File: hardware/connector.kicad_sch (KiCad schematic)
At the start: 2 parts

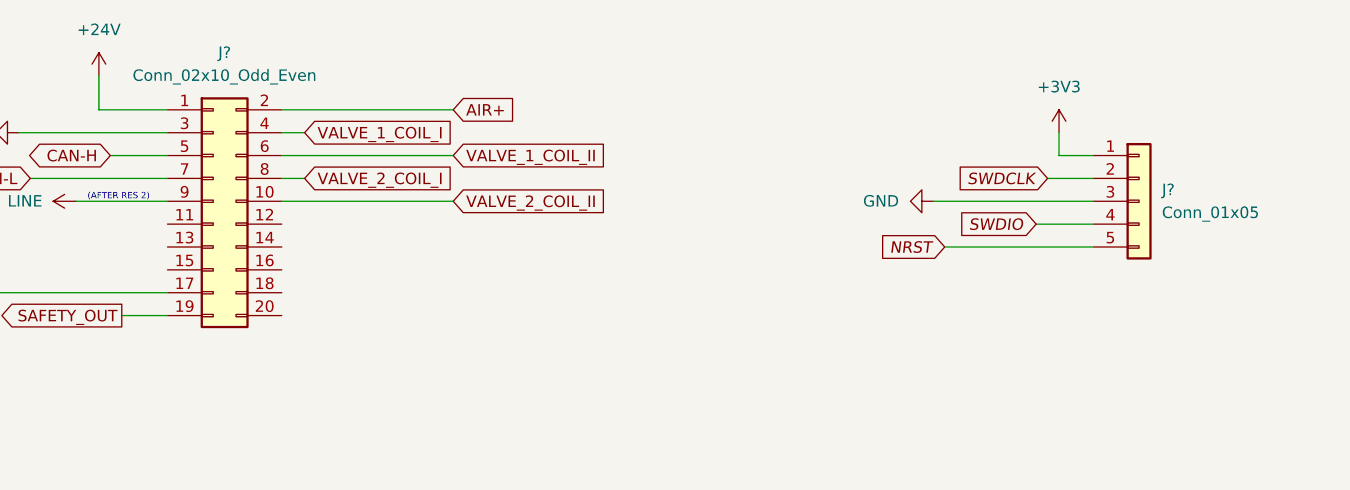
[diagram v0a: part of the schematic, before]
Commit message: Schematic ready for second review
Cleaned up, numerated, added footprints, JW notes considered
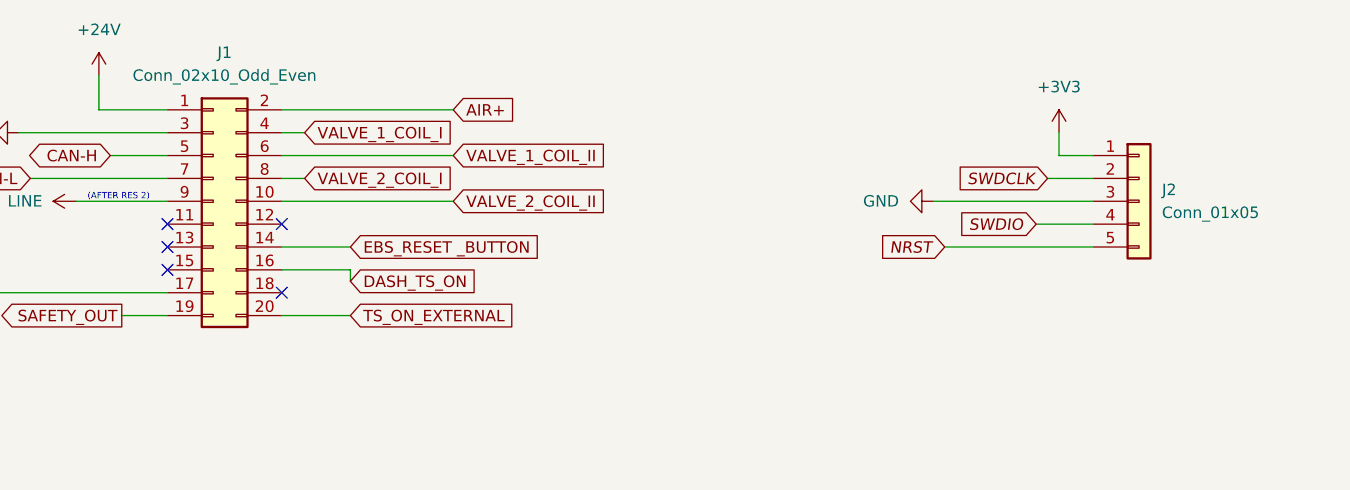
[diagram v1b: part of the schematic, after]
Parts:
- gave numbers to parts that had none: 2
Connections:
- net EBS_RESET _BUTTON: now reaches J1.14 (Pin_14)
- net DASH_TS_ON: now reaches J1.16 (Pin_16)
- net TS_ON_EXTERNAL: now reaches J1.20 (Pin_20)
- no-connect marks 0 -> 5
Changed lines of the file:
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@@
     (company "PUT Motorsport")
   )
+  (no_connect (at 128.27 92.71))
+  (no_connect (at 128.27 85.09))
+  (no_connect (at 115.57 85.09))
+  (no_connect (at 115.57 87.63))
+  (no_connect (at 115.57 90.17))
   (wire (pts (xy 128.27 77.47) (xy 147.32 77.47))
     (stroke (width 0) (type default) (color 0 0 0 0))
@@
     (stroke (width 0) (type default) (color 0 0 0 0))
   )
+  (wire (pts (xy 128.27 95.25) (xy 135.89 95.25))
+    (stroke (width 0) (type default) (color 0 0 0 0))
+  )
   (wire (pts (xy 99.06 74.93) (xy 115.57 74.93))
     (stroke (width 0) (type default) (color 0 0 0 0))
   )
+  (wire (pts (xy 128.27 90.17) (xy 135.89 90.17))
+    (stroke (width 0) (type default) (color 0 0 0 0))
+  )
   (wire (pts (xy 218.44 77.47) (xy 214.63 77.47))
     (stroke (width 0) (type default) (color 0 0 0 0))
@@
   )
   (wire (pts (xy 212.09 85.09) (xy 218.44 85.09))
+    (stroke (width 0) (type default) (color 0 0 0 0))
+  )
+  (wire (pts (xy 128.27 87.63) (xy 135.89 87.63))
+    (stroke (width 0) (type default) (color 0 0 0 0))
+  )
+  (wire (pts (xy 135.89 90.17) (xy 135.89 91.44))
     (stroke (width 0) (type default) (color 0 0 0 0))
   )
@@
     )
   )
+  (global_label "DASH_TS_ON" (shape input) (at 135.89 91.44 0) (fields_autoplaced)
+    (effects (font (size 1.27 1.27)) (justify left))
+    (property "Intersheet References" "${INTERSHEET_REFS}" (id 0) (at 149.975 91.5194 0)
+      (effects (font (size 1.27 1.27)) (justify left) hide)
+    )
+  )
   (global_label "VALVE_1_COIL_I" (shape input) (at 130.81 74.93 0) (fields_autoplaced)
     (effects (font (size 1.27 1.27)) (justify left))
@@
     )
   )
+  (global_label "TS_ON_EXTERNAL" (shape input) (at 135.89 95.25 0) (fields_autoplaced)
+    (effects (font (size 1.27 1.27)) (justify left))
+    (property "Intersheet References" "${INTERSHEET_REFS}" (id 0) (at 154.2688 95.3294 0)
+      (effects (font (size 1.27 1.27)) (justify left) hide)
+    )
+  )
+  (global_label "EBS_RESET _BUTTON" (shape input) (at 135.89 87.63 0) (fields_autoplaced)
+    (effects (font (size 1.27 1.27)) (justify left))
+    (property "Intersheet References" "${INTERSHEET_REFS}" (id 0) (at 157.7764 87.7094 0)
+      (effects (font (size 1.27 1.27)) (justify left) hide)
+    )
+  )
   (global_label "SAFETY_OUT" (shape output) (at 110.49 95.25 180) (fields_autoplaced)
     (effects (font (size 1.27 1.27)) (justify right))
@@
   (symbol (lib_id "power:+3V3") (at 214.63 74.93 0) (unit 1)
     (in_bom yes) (on_board yes) (fields_autoplaced)
-    (property "Reference" "#PWR?" (id 0) (at 214.63 78.74 0)
+    (property "Reference" "#PWR049" (id 0) (at 214.63 78.74 0)
       (effects (font (size 1.27 1.27)) hide)
     )
@@
   (symbol (lib_id "power:+24V") (at 107.95 68.58 0) (unit 1)
     (in_bom yes) (on_board yes) (fields_autoplaced)
-    (property "Reference" "#PWR?" (id 0) (at 107.95 72.39 0)
+    (property "Reference" "#PWR047" (id 0) (at 107.95 72.39 0)
       (effects (font (size 1.27 1.27)) hide)
     )
@@
   (symbol (lib_id "power:LINE") (at 105.41 82.55 90) (unit 1)
     (in_bom yes) (on_board yes)
-    (property "Reference" "#PWR?" (id 0) (at 109.22 82.55 0)
+    (property "Reference" "#PWR046" (id 0) (at 109.22 82.55 0)
       (effects (font (size 1.27 1.27)) hide)
     )
@@
   (symbol (lib_id "Connector_Generic:Conn_01x05") (at 223.52 82.55 0) (unit 1)
     (in_bom yes) (on_board yes) (fields_autoplaced)
-    (property "Reference" "J?" (id 0) (at 226.06 81.2799 0)
+    (property "Reference" "J2" (id 0) (at 226.06 81.2799 0)
       (effects (font (size 1.27 1.27)) (justify left))
     )
@@
   (symbol (lib_id "Connector_Generic:Conn_02x10_Odd_Even") (at 120.65 82.55 0) (unit 1)
     (in_bom yes) (on_board yes) (fields_autoplaced)
-    (property "Reference" "J?" (id 0) (at 121.92 66.04 0))
+    (property "Reference" "J1" (id 0) (at 121.92 66.04 0))
     (property "Value" "Conn_02x10_Odd_Even" (id 1) (at 121.92 68.58 0))
     (property "Footprint" "" (id 2) (at 120.65 82.55 0)
@@
   (symbol (lib_id "power:GND") (at 200.66 82.55 270) (unit 1)
     (in_bom yes) (on_board yes) (fields_autoplaced)
-    (property "Reference" "#PWR?" (id 0) (at 194.31 82.55 0)
+    (property "Reference" "#PWR048" (id 0) (at 194.31 82.55 0)
       (effects (font (size 1.27 1.27)) hide)
     )
@@
   (symbol (lib_id "power:GND") (at 99.06 74.93 270) (unit 1)
     (in_bom yes) (on_board yes) (fields_autoplaced)
-    (property "Reference" "#PWR?" (id 0) (at 92.71 74.93 0)
-      (effects (font (size 1.27 1.27)) hide)
-    )
+    (property "Reference" "#PWR045" (id 0) (at 92.71 74.93 0)
+      (effects (font (size 1.27 1.27)) hide)
+    )

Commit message: working simulations, assigned footprints
"nightly" relase
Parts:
- J1: value Conn_02x10_Odd_Even -> Conn_02x11_Odd_Even; symbol Connector_Generic:Conn_02x10_Odd_Even -> Connector_Generic:Conn_02x11_Odd_Even
- J2: footprint (none) -> Connector_PinHeader_2.54mm:PinHeader_1x05_P2.54mm_Vertical
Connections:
- net +24V: now also J1.3 (Pin_3); no longer J1.1 (Pin_1)
- net AIR+: now also J1.4 (Pin_4); no longer J1.2 (Pin_2)
- net CAN-H: now also J1.22 (Pin_22); no longer J1.5 (Pin_5)
- net CAN-L: now also J1.21 (Pin_21); no longer J1.7 (Pin_7)
- net DASH_TS_ON: now also J1.18 (Pin_18); no longer J1.16 (Pin_16)
- net EBS_RESET _BUTTON: now also J1.16 (Pin_16); no longer J1.14 (Pin_14)
- net GND: now also J1.5 (Pin_5); no longer J1.3 (Pin_3)
- net LINE: now also J1.11 (Pin_11); no longer J1.9 (Pin_9)
- net SAFETY_IN: now also J1.19 (Pin_19); no longer J1.17 (Pin_17)
- net SAFETY_OUT: now also J1.1 (Pin_1); no longer J1.19 (Pin_19)
- net TS_ON_EXTERNAL: now also J1.2 (Pin_2); no longer J1.20 (Pin_20)
- net VALVE_1_COIL_I: now also J1.6 (Pin_6); no longer J1.4 (Pin_4)
- net VALVE_1_COIL_II: now also J1.8 (Pin_8); no longer J1.6 (Pin_6)
- net VALVE_2_COIL_I: now also J1.10 (Pin_10); no longer J1.8 (Pin_8)
- net VALVE_2_COIL_II: now also J1.12 (Pin_12); no longer J1.10 (Pin_10)
- net AIR_EBS: now reaches J1.13 (Pin_13)
- net AIR_REDUNDANT: now reaches J1.15 (Pin_15)
- new net AIR_MAIN: J1.17 (Pin_17)
- new net AUX1: J1.14 (Pin_14)
- new net AUX2: J1.20 (Pin_20)
- no-connect marks 5 -> 2

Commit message: kończymy balet na dziś
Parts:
- removed J1: Conn_02x11_Odd_Even, symbol Connector_Generic:Conn_02x11_Odd_Even
- added J1: SAFETY_SUPPLY, PUTM_Kicad_FOOTPRINTS:M80-5L104YYMC, symbol Connector_Generic:Conn_01x04
- added J3: SENSORS, PUTM_Kicad_FOOTPRINTS:M80-5L104YYMC, symbol Connector_Generic:Conn_01x04
- added J4: VALVES, PUTM_Kicad_FOOTPRINTS:M80-5L104YYMC, symbol Connector_Generic:Conn_01x04
- added J5: MAIN, PUTM_Kicad_FOOTPRINTS:M80-5L112YYMC, symbol Connector_Generic:Conn_01x12
- J2: value Conn_01x05 -> SWDIO_CONN
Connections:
- net +24V: now also J5.4 (Pin_4)
- net AIR+: now also J5.3 (Pin_3)
- net AIR_EBS: now also J3.2 (Pin_2)
- net AIR_MAIN: now also J3.1 (Pin_1)
- net AIR_REDUNDANT: now also J3.3 (Pin_3)
- net AUX1: now also J5.6 (Pin_6)
- net AUX2: now also J5.9 (Pin_9)
- net CAN-H: now also J5.10 (Pin_10)
- net CAN-L: now also J5.11 (Pin_11)
- net DASH_TS_ON: now also J5.8 (Pin_8)
- net EBS_RESET _BUTTON: now also J5.7 (Pin_7)
- net GND: now also J5.5 (Pin_5)
- net LINE: now also J1.1 (Pin_1)
- net SAFETY_IN: now also J1.2 (Pin_2)
- net SAFETY_OUT: now also J1.3 (Pin_3)
- net TS_ON_EXTERNAL: now also J5.2 (Pin_2)
- net VALVE_1_COIL_I: now also J4.1 (Pin_1)
- net VALVE_1_COIL_II: now also J4.2 (Pin_2)
- net VALVE_2_COIL_I: now also J4.3 (Pin_3)
- net VALVE_2_COIL_II: now also J4.4 (Pin_4)
- no-connect marks 2 -> 4
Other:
- note added: "10pin version not in stock ;/"
- note added: "Connectors are divided intentionaly- Clue is to speed up inspection process where scrutineer will be unplugging different things and checking functional safety of the system"
- note added: "HARWIN J-TEK"
- note added: "M80-5L10442MC"
- note added: "M80-5L11242MC"
- note added: "so they are divided to sections to speed it up"
- note removed: "konektory dodam jak będe wiedział jak chce żeby PCB wyglądał"

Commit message: dobra ide spać
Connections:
- net VALVE_1_COIL_II: now also J4.3 (Pin_3); no longer J4.2 (Pin_2)
- net VALVE_2_COIL_I: now also J4.2 (Pin_2); no longer J4.3 (Pin_3)
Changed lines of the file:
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@@
+    )
+  )
+  (global_label "VALVE_2_COIL_I" (shape input) (at 99.06 97.79 180) (fields_autoplaced)
+    (effects (font (size 1.27 1.27)) (justify right))
+    (property "Intersheet References" "${INTERSHEET_REFS}" (id 0) (at 82.2536 97.7106 0)
+      (effects (font (size 1.27 1.27)) (justify right) hide)
     )
   )
@@
     )
   )
-  (global_label "VALVE_1_COIL_II" (shape input) (at 99.06 97.79 180) (fields_autoplaced)
-    (effects (font (size 1.27 1.27)) (justify right))
-    (property "Intersheet References" "${INTERSHEET_REFS}" (id 0) (at 81.6488 97.7106 0)
-      (effects (font (size 1.27 1.27)) (justify right) hide)
-    )
-  )
   (global_label "AIR_REDUNDANT" (shape input) (at 120.65 85.09 180) (fields_autoplaced)
     (effects (font (size 1.27 1.27)) (justify right))
@@
     )
   )
-  (global_label "VALVE_2_COIL_I" (shape input) (at 115.57 100.33 180) (fields_autoplaced)
+  (global_label "VALVE_1_COIL_II" (shape input) (at 115.57 100.33 180) (fields_autoplaced)
     (effects (font (size 1.27 1.27)) (justify right))
-    (property "Intersheet References" "${INTERSHEET_REFS}" (id 0) (at 98.7636 100.2506 0)
+    (property "Intersheet References" "${INTERSHEET_REFS}" (id 0) (at 98.1588 100.2506 0)
       (effects (font (size 1.27 1.27)) (justify right) hide)
     )

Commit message: full 3d models, pre-routing, corrections
kurwa bezpiecznik od wczoraj a fura dalej nie jeździ siedze u rakietowcow bo cieplo chlopaki co z wami
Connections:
- net CAN-H is gone; now on net AUX1: J5.10 (Pin_10)
- net +24V: now also J5.5 (Pin_5); no longer J5.4 (Pin_4)
- net AIR+: now also J5.12 (Pin_12); no longer J5.3 (Pin_3)
- net AUX1: no longer J5.6 (Pin_6)
- net DASH_TS_ON: now also J5.2 (Pin_2); no longer J5.8 (Pin_8)
- net EBS_RESET _BUTTON: now also J5.8 (Pin_8); no longer J5.7 (Pin_7)
- net GND: now also J5.6 (Pin_6); no longer J5.5 (Pin_5)
- net TS_ON_EXTERNAL: now also J5.3 (Pin_3); no longer J5.2 (Pin_2)
- net CAN-: now reaches J5.1 (Pin_1)
- net CAN-L: no longer names the net of J5.11 (Pin_11)
- new net CAN+: J5.7 (Pin_7)

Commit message: fixed references addet tp;s mam pojutrze przejebany egzamin nara
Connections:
- net AIR_EBS: now also J3.1 (Pin_1); no longer J3.2 (Pin_2)
- net AIR_MAIN: now also J3.2 (Pin_2); no longer J3.1 (Pin_1)
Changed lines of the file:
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@@
+    )
+  )
+  (global_label "AIR_MAIN" (shape input) (at 101.6 82.55 180) (fields_autoplaced)
+    (effects (font (size 1.27 1.27)) (justify right))
+    (property "Intersheet References" "${INTERSHEET_REFS}" (id 0) (at 90.7807 82.4706 0)
+      (effects (font (size 1.27 1.27)) (justify right) hide)
     )
   )
@@
     )
   )
-  (global_label "AIR_MAIN" (shape input) (at 116.84 80.01 180) (fields_autoplaced)
+  (global_label "AIR_EBS" (shape input) (at 116.84 80.01 180) (fields_autoplaced)
     (effects (font (size 1.27 1.27)) (justify right))
-    (property "Intersheet References" "${INTERSHEET_REFS}" (id 0) (at 106.0207 79.9306 0)
+    (property "Intersheet References" "${INTERSHEET_REFS}" (id 0) (at 106.8674 79.9306 0)
       (effects (font (size 1.27 1.27)) (justify right) hide)
     )
@@
       (effects (font (size 1.27 1.27)) (justify right) hide)
     )
-  )
-  (global_label "AIR_EBS" (shape input) (at 101.6 82.55 180) (fields_autoplaced)
-    (effects (font (size 1.27 1.27)) (justify right))
-    (property "Intersheet References" "${INTERSHEET_REFS}" (id 0) (at 91.6274 82.4706 0)
-      (effects (font (size 1.27 1.27)) (justify right) hide)
-    )

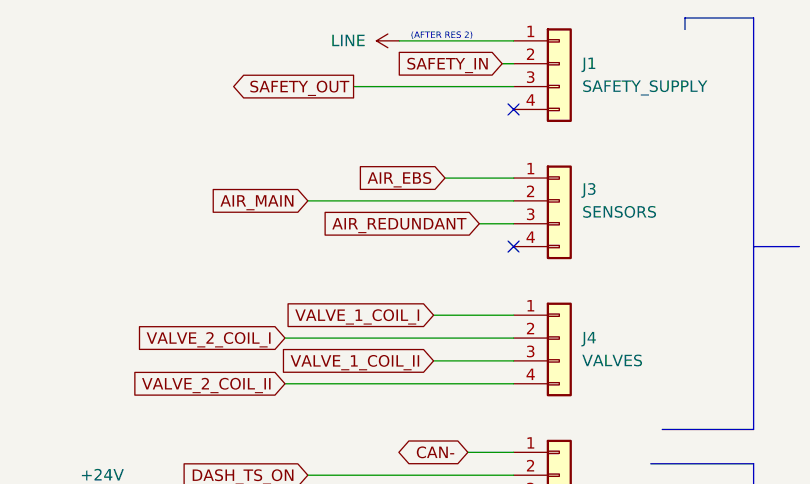
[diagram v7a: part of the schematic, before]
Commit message: routing update, new supply section routed
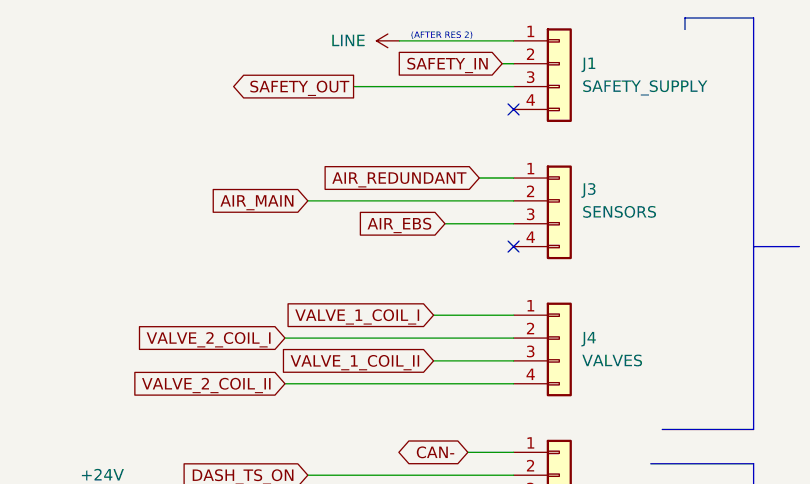
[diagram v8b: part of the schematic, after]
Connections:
- net AIR_EBS: now also J3.3 (Pin_3); no longer J3.1 (Pin_1)
- net AIR_REDUNDANT: now also J3.1 (Pin_1); no longer J3.3 (Pin_3)
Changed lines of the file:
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@@
+    (stroke (width 0) (type default) (color 0 0 0 0))
+  )
+  (wire (pts (xy 120.65 80.01) (xy 124.46 80.01))
     (stroke (width 0) (type default) (color 0 0 0 0))
   )
@@
     (stroke (width 0) (type default) (color 0 0 0 0))
   )
-  (wire (pts (xy 120.65 85.09) (xy 124.46 85.09))
+  (wire (pts (xy 116.84 85.09) (xy 124.46 85.09))
     (stroke (width 0) (type default) (color 0 0 0 0))
   )
@@
   )
   (polyline (pts (xy 151.13 137.16) (xy 151.13 124.46))
-    (stroke (width 0) (type default) (color 0 0 0 0))
-  )
-  (wire (pts (xy 116.84 80.01) (xy 124.46 80.01))
     (stroke (width 0) (type default) (color 0 0 0 0))
   )
@@
     )
   )
-  (global_label "AIR_EBS" (shape input) (at 116.84 80.01 180) (fields_autoplaced)
-    (effects (font (size 1.27 1.27)) (justify right))
-    (property "Intersheet References" "${INTERSHEET_REFS}" (id 0) (at 106.8674 79.9306 0)
-      (effects (font (size 1.27 1.27)) (justify right) hide)
-    )
-  )
   (global_label "DASH_TS_ON" (shape input) (at 101.6 113.03 180) (fields_autoplaced)
     (effects (font (size 1.27 1.27)) (justify right))
@@
     )
   )
+  (global_label "AIR_EBS" (shape input) (at 116.84 85.09 180) (fields_autoplaced)
+    (effects (font (size 1.27 1.27)) (justify right))
+    (property "Intersheet References" "${INTERSHEET_REFS}" (id 0) (at 106.8674 85.0106 0)
+      (effects (font (size 1.27 1.27)) (justify right) hide)
+    )
+  )
   (global_label "VALVE_2_COIL_II" (shape input) (at 99.06 102.87 180) (fields_autoplaced)
     (effects (font (size 1.27 1.27)) (justify right))
@@
     )
   )
-  (global_label "AIR_REDUNDANT" (shape input) (at 120.65 85.09 180) (fields_autoplaced)
-    (effects (font (size 1.27 1.27)) (justify right))
-    (property "Intersheet References" "${INTERSHEET_REFS}" (id 0) (at 103.2993 85.0106 0)
-      (effects (font (size 1.27 1.27)) (justify right) hide)
-    )
-  )
   (global_label "VALVE_1_COIL_II" (shape input) (at 115.57 100.33 180) (fields_autoplaced)
     (effects (font (size 1.27 1.27)) (justify right))
@@
       (effects (font (size 1.27 1.27)) (justify right) hide)
     )
+  )
+  (global_label "AIR_REDUNDANT" (shape input) (at 120.65 80.01 180) (fields_autoplaced)
+    (effects (font (size 1.27 1.27)) (justify right))
+    (property "Intersheet References" "${INTERSHEET_REFS}" (id 0) (at 103.2993 79.9306 0)
+      (effects (font (size 1.27 1.27)) (justify right) hide)
+    )
